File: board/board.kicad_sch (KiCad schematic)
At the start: 6 parts, among them J2 100_digital_IO, J3 SWD_6_Pol_Needle, J4 100_digital_IO

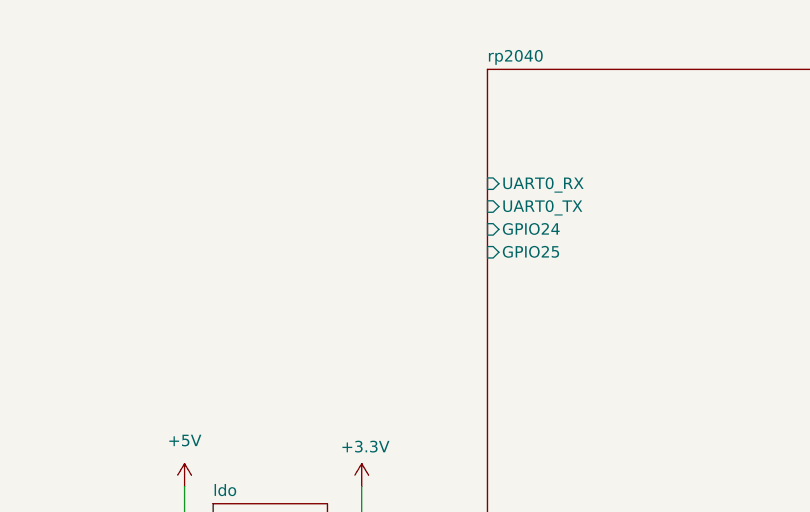
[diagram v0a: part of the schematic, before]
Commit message: added boot select button
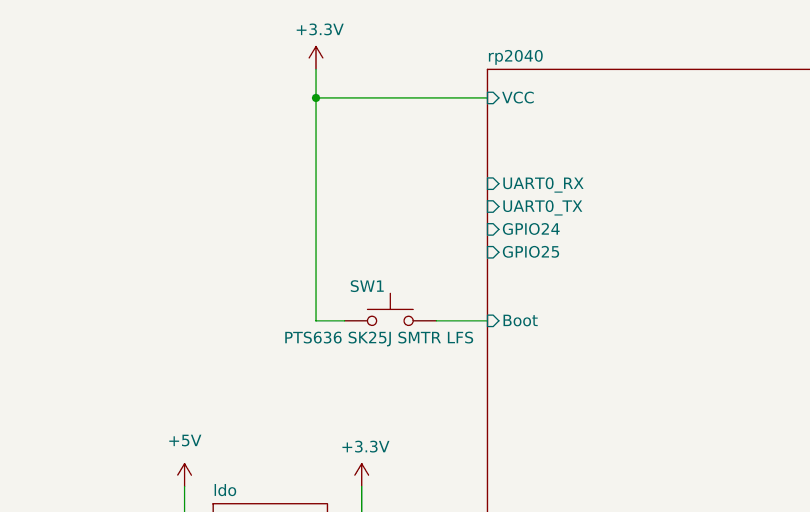
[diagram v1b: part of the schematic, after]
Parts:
- added SW1: PTS636 SK25J SMTR LFS, Resistor_SMD:R_2512_6332Metric, symbol Switch:SW_Push
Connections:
- net +3V3: now also SW1.1
- new net rp2040/Boot: SW1.2
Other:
- sheet rp2040 ports: added Boot, VCC; removed none
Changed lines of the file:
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@@
   (junction (at 74.295 100.965) (diameter 0) (color 0 0 0 0)
+  )
+  (junction (at 86.36 25.4) (diameter 0) (color 0 0 0 0)
   )
   (junction (at 71.755 73.025) (diameter 0) (color 0 0 0 0)
@@
     (stroke (width 0) (type default))
   )
+  (wire (pts (xy 86.36 22.225) (xy 86.36 25.4))
+    (stroke (width 0) (type default))
+  )
   (wire (pts (xy 167.64 43.815) (xy 227.33 43.815))
     (stroke (width 0) (type default))
@@
     (stroke (width 0) (type default))
   )
+  (wire (pts (xy 86.36 25.4) (xy 105.41 25.4))
+    (stroke (width 0) (type default))
+  )
   (wire (pts (xy 74.295 100.965) (xy 74.295 78.105))
     (stroke (width 0) (type default))
@@
     (stroke (width 0) (type default))
   )
+  (wire (pts (xy 89.535 50.165) (xy 86.36 50.165))
+    (stroke (width 0) (type default))
+  )
   (wire (pts (xy 48.895 151.765) (xy 48.895 146.685))
     (stroke (width 0) (type default))
@@
     (stroke (width 0) (type default))
   )
+  (wire (pts (xy 99.695 50.165) (xy 105.41 50.165))
+    (stroke (width 0) (type default))
+  )
   (wire (pts (xy 32.385 149.225) (xy 51.435 149.225))
     (stroke (width 0) (type default))
@@
   )
   (wire (pts (xy 189.23 46.355) (xy 225.425 46.355))
+    (stroke (width 0) (type default))
+  )
+  (wire (pts (xy 86.36 50.165) (xy 86.36 25.4))
     (stroke (width 0) (type default))
   )
@@
         (path "/57732dd3-1162-4c3f-88bd-31bf473d124d"
           (reference "J3") (unit 1)
+        )
+      )
+    )
+  )
+  (symbol (lib_id "Switch:SW_Push") (at 94.615 50.165 0) (unit 1)
+    (in_bom yes) (on_board yes) (dnp no)
+    (property "Reference" "SW1" (at 92.075 46.355 0)
+      (effects (font (size 1.27 1.27)))
+    )
+    (property "Value" "PTS636 SK25J SMTR LFS" (at 93.345 52.07 0)
+      (effects (font (size 1.27 1.27)))
+    )
+    (property "Footprint" "Resistor_SMD:R_2512_6332Metric" (at 94.615 45.085 0)
+      (effects (font (size 1.27 1.27)) hide)
+    )
+    (property "Datasheet" "~" (at 94.615 45.085 0)
+      (effects (font (size 1.27 1.27)) hide)
+    )
+    (property "MPN" "PTS636 SK25J SMTR LFS" (at 94.615 50.165 0)
+      (effects (font (size 1.27 1.27)) hide)
+    )
+    (pin "1")
+    (pin "2")
+    (instances
+      (project "board"
+        (path "/57732dd3-1162-4c3f-88bd-31bf473d124d"
+          (reference "SW1") (unit 1)
         )
       )
@@
     )
   )
+  (symbol (lib_id "power:+3.3V") (at 86.36 22.225 0) (unit 1)
+    (in_bom yes) (on_board yes) (dnp no)
+    (property "Reference" "#PWR010" (at 86.36 26.035 0)
+      (effects (font (size 1.27 1.27)) hide)
+    )
+    (property "Value" "+3.3V" (at 86.741 17.8308 0)
+      (effects (font (size 1.27 1.27)))
+    )
+    (property "Footprint" "" (at 86.36 22.225 0)
+      (effects (font (size 1.27 1.27)) hide)
+    )
+    (property "Datasheet" "" (at 86.36 22.225 0)
+      (effects (font (size 1.27 1.27)) hide)
+    )
+    (pin "1")
+    (instances
+      (project "board"
+        (path "/57732dd3-1162-4c3f-88bd-31bf473d124d/d7f4faf0-6611-4124-99f4-3c5e31784302"
+          (reference "#PWR010") (unit 1)
+        )
+        (path "/57732dd3-1162-4c3f-88bd-31bf473d124d"
+          (reference "#PWR01") (unit 1)
+        )
+      )
+    )
+  )
   (symbol (lib_id "power:GND") (at 250.825 100.33 0) (unit 1)
     (in_bom yes) (on_board yes) (dnp no)
@@
       (effects (font (size 1.27 1.27)) (justify left))
     )
+    (pin "VCC" input (at 105.41 25.4 180)
+      (effects (font (size 1.27 1.27)) (justify left))
+    )
+    (pin "Boot" input (at 105.41 50.165 180)
+      (effects (font (size 1.27 1.27)) (justify left))
+    )

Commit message: fixed boot select circuit
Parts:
- added R1: 1k, Resistor_SMD:R_0603_1608Metric, symbol Device:R_Small
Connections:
- net +3V3: no longer SW1.1
- net GND: now also SW1.1
- net rp2040/Boot: now also R1.2; no longer SW1.2
- new net: R1.1, SW1.2
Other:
- moved on the sheet: SW1
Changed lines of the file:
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@@
   (junction (at 74.295 100.965) (diameter 0) (color 0 0 0 0)
-  )
-  (junction (at 86.36 25.4) (diameter 0) (color 0 0 0 0)
   )
   (junction (at 71.755 73.025) (diameter 0) (color 0 0 0 0)
@@
     (stroke (width 0) (type default))
   )
+  (wire (pts (xy 101.6 50.165) (xy 105.41 50.165))
+    (stroke (width 0) (type default))
+  )
   (wire (pts (xy 74.295 100.965) (xy 70.485 100.965))
     (stroke (width 0) (type default))
   )
-  (wire (pts (xy 89.535 50.165) (xy 86.36 50.165))
-    (stroke (width 0) (type default))
-  )
   (wire (pts (xy 48.895 151.765) (xy 48.895 146.685))
     (stroke (width 0) (type default))
@@
     (stroke (width 0) (type default))
   )
-  (wire (pts (xy 99.695 50.165) (xy 105.41 50.165))
+  (wire (pts (xy 79.375 50.165) (xy 81.28 50.165))
     (stroke (width 0) (type default))
   )
@@
     (stroke (width 0) (type default))
   )
-  (wire (pts (xy 86.36 50.165) (xy 86.36 25.4))
-    (stroke (width 0) (type default))
-  )
   (wire (pts (xy 229.235 83.185) (xy 229.235 41.275))
     (stroke (width 0) (type default))
@@
     (stroke (width 0) (type default))
   )
+  (wire (pts (xy 79.375 54.61) (xy 79.375 50.165))
+    (stroke (width 0) (type default))
+  )
   (wire (pts (xy 250.825 55.245) (xy 250.825 58.42))
     (stroke (width 0) (type default))
@@
   )
   (wire (pts (xy 74.295 107.95) (xy 74.295 100.965))
+    (stroke (width 0) (type default))
+  )
+  (wire (pts (xy 91.44 50.165) (xy 96.52 50.165))
     (stroke (width 0) (type default))
   )
@@
     )
   )
-  (symbol (lib_id "Switch:SW_Push") (at 94.615 50.165 0) (unit 1)
+  (symbol (lib_id "Switch:SW_Push") (at 86.36 50.165 0) (unit 1)
     (in_bom yes) (on_board yes) (dnp no)
-    (property "Reference" "SW1" (at 92.075 46.355 0)
-      (effects (font (size 1.27 1.27)))
-    )
-    (property "Value" "PTS636 SK25J SMTR LFS" (at 93.345 52.07 0)
-      (effects (font (size 1.27 1.27)))
-    )
-    (property "Footprint" "Resistor_SMD:R_2512_6332Metric" (at 94.615 45.085 0)
-      (effects (font (size 1.27 1.27)) hide)
-    )
-    (property "Datasheet" "~" (at 94.615 45.085 0)
-      (effects (font (size 1.27 1.27)) hide)
-    )
-    (property "MPN" "PTS636 SK25J SMTR LFS" (at 94.615 50.165 0)
+    (property "Reference" "SW1" (at 83.82 46.355 0)
+      (effects (font (size 1.27 1.27)))
+    )
+    (property "Value" "PTS636 SK25J SMTR LFS" (at 85.09 52.07 0)
+      (effects (font (size 1.27 1.27)))
+    )
+    (property "Footprint" "Resistor_SMD:R_2512_6332Metric" (at 86.36 45.085 0)
+      (effects (font (size 1.27 1.27)) hide)
+    )
+    (property "Datasheet" "~" (at 86.36 45.085 0)
+      (effects (font (size 1.27 1.27)) hide)
+    )
+    (property "MPN" "PTS636 SK25J SMTR LFS" (at 86.36 50.165 0)
       (effects (font (size 1.27 1.27)) hide)
     )
@@
     )
   )
+  (symbol (lib_id "Device:R_Small") (at 99.06 50.165 90) (mirror x) (unit 1)
+    (in_bom yes) (on_board yes) (dnp no)
+    (property "Reference" "R1" (at 99.695 48.26 90)
+      (effects (font (size 1.27 1.27)))
+    )
+    (property "Value" "1k" (at 99.06 53.975 90)
+      (effects (font (size 1.27 1.27)))
+    )
+    (property "Footprint" "Resistor_SMD:R_0603_1608Metric" (at 99.06 50.165 0)
+      (effects (font (size 1.27 1.27)) hide)
+    )
+    (property "Datasheet" "~" (at 99.06 50.165 0)
+      (effects (font (size 1.27 1.27)) hide)
+    )
+    (pin "1")
+    (pin "2")
+    (instances
+      (project "board"
+        (path "/57732dd3-1162-4c3f-88bd-31bf473d124d"
+          (reference "R1") (unit 1)
+        )
+      )
+    )
+  )
   (symbol (lib_id "power:+3.3V") (at 32.385 146.685 0) (unit 1)
     (in_bom yes) (on_board yes) (dnp no)
@@
         )
       )
+    )
+  )
+  (symbol (lib_id "power:GND") (at 79.375 54.61 0) (unit 1)
+    (in_bom yes) (on_board yes) (dnp no) (fields_autoplaced)
+    (property "Reference" "#PWR02" (at 79.375 60.96 0)
+      (effects (font (size 1.27 1.27)) hide)
+    )
+    (property "Value" "GND" (at 79.375 59.69 0)
+      (effects (font (size 1.27 1.27)))
+    )
+    (property "Footprint" "" (at 79.375 54.61 0)
+      (effects (font (size 1.27 1.27)) hide)
+    )
+    (property "Datasheet" "" (at 79.375 54.61 0)
+      (effects (font (size 1.27 1.27)) hide)
+    )
+    (pin "1")
+    (instances
+      (project "board"
+        (path "/57732dd3-1162-4c3f-88bd-31bf473d124d"
+          (reference "#PWR02") (unit 1)
+        )
+      )

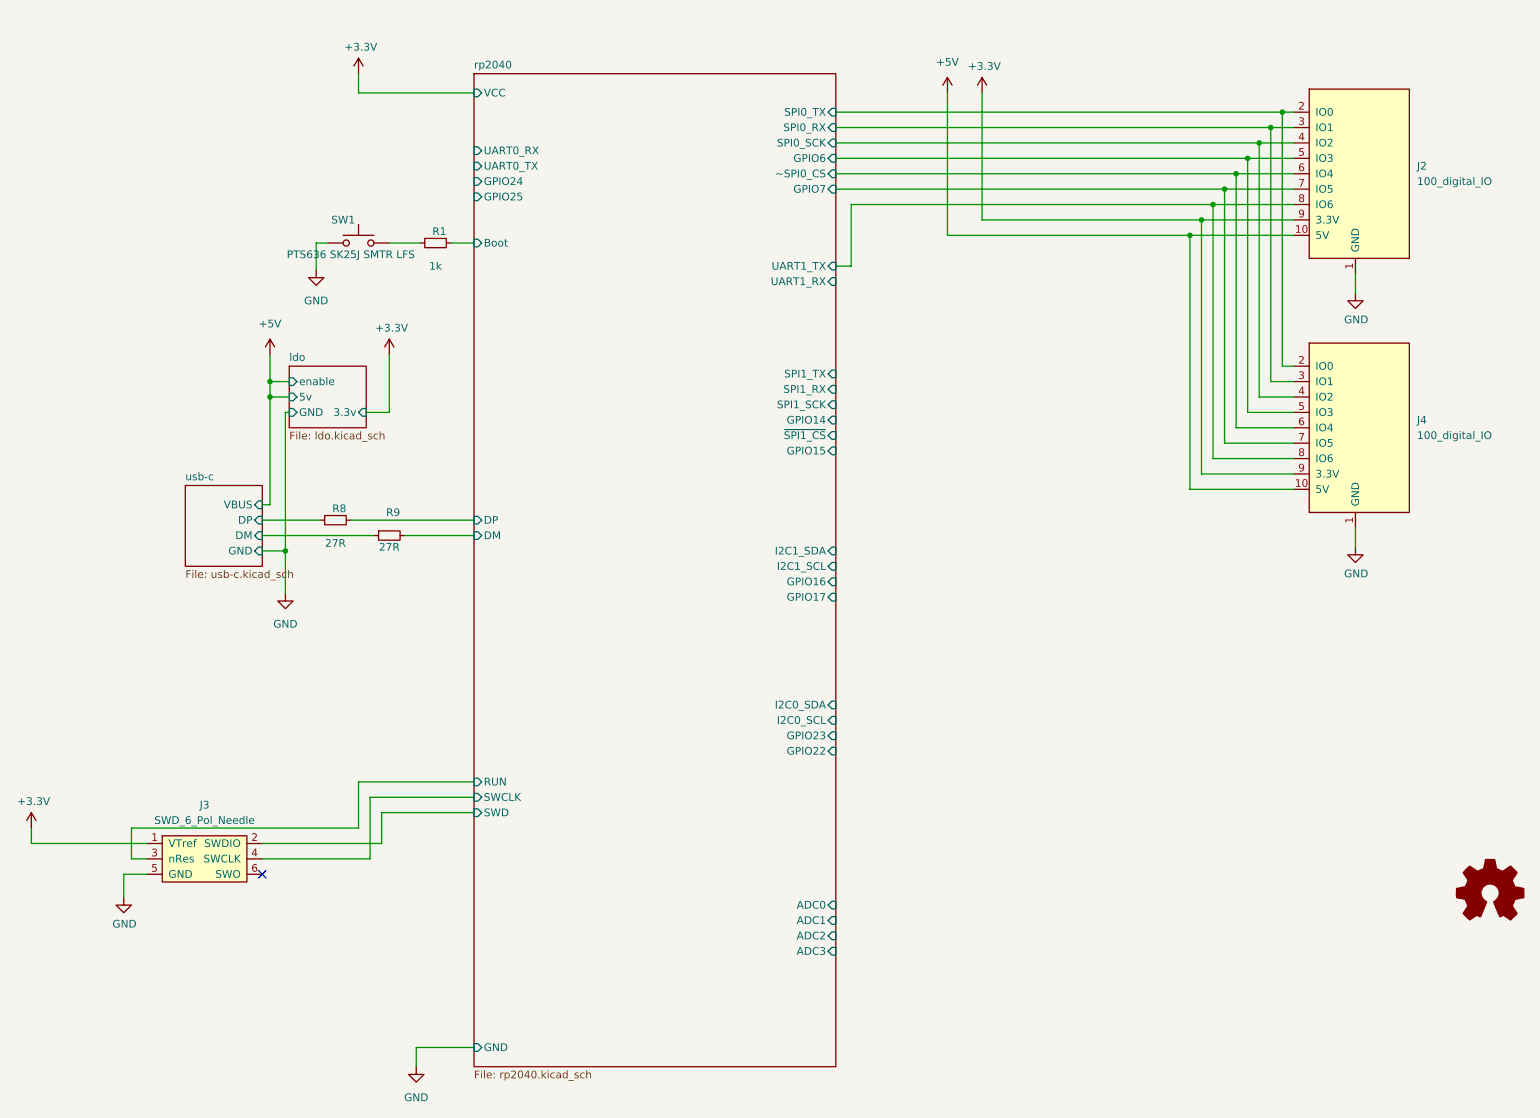
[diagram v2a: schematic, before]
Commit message: added straping support for different interfaces
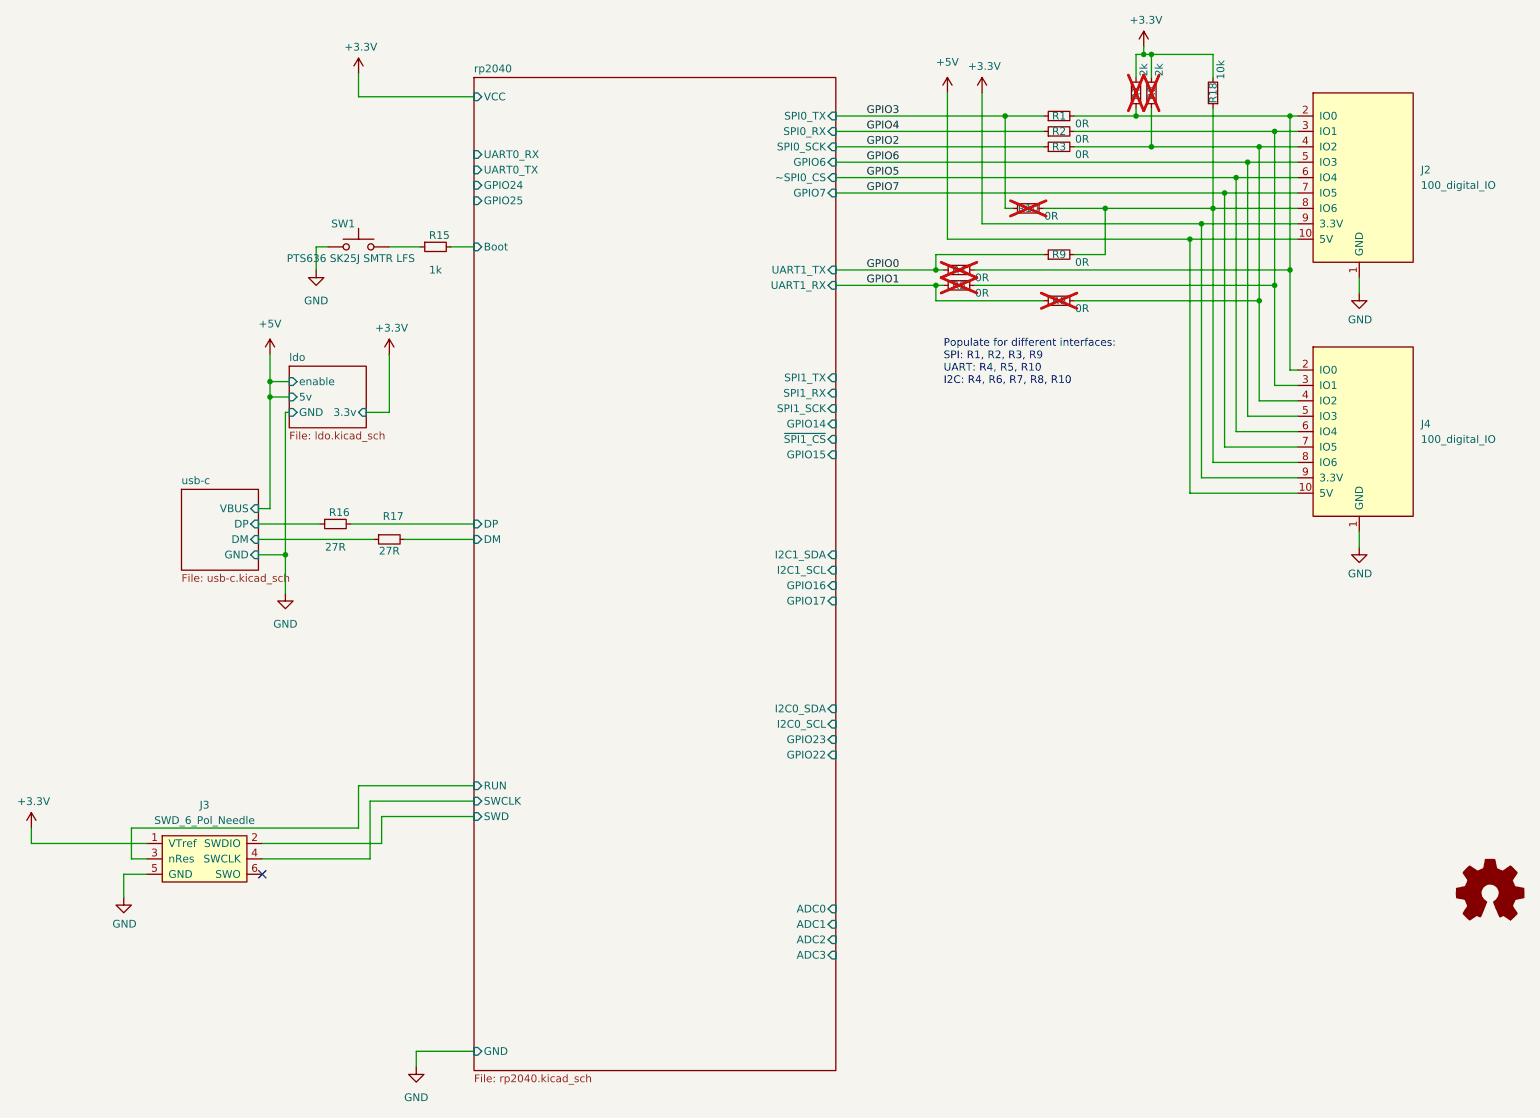
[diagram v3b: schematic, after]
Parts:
- added R1, R10, R2, R3, R4, R5, R6, R9: 0R, Resistor_SMD:R_0603_1608Metric, symbol Device:R_Small
- added R18: 10k, Resistor_SMD:R_0603_1608Metric, symbol Device:R_Small
- added R7, R8: 2k, Resistor_SMD:R_0603_1608Metric, symbol Device:R_Small
- renumbered R1 to R15, R8 to R16, R9 to R17
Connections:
- net +3V3: now also R18.2, R7.2, R8.2
- net rp2040/GPIO6 renamed GPIO6
- net rp2040/GPIO7 renamed GPIO7
- net rp2040/SPI0_RX: no longer names the net of J2.3 (IO1), J4.3 (IO1)
- net rp2040/SPI0_RX: now also R2.2, R5.2
- net rp2040/SPI0_SCK: no longer names the net of J2.4 (IO2), J4.4 (IO2)
- net rp2040/SPI0_SCK: now also R3.2, R6.2, R8.1
- net rp2040/SPI0_TX: no longer names the net of J2.2 (IO0), J4.2 (IO0)
- net rp2040/SPI0_TX: now also R1.2, R4.2, R7.1
- net rp2040/UART1_TX: no longer names the net of J2.8 (IO6), J4.8 (IO6)
- net rp2040/UART1_TX: now also R10.2, R18.1, R9.2
- net rp2040/~SPI0_CS renamed GPIO5
- new net GPIO0: R4.1, R9.1
- new net GPIO1: R5.1, R6.1
- new net GPIO2: R3.1
- new net GPIO3: R1.1, R10.1
- new net GPIO4: R2.1
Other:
- note added: "Populate for different interfaces: SPI: R1, R2, R3, R9 UART: R4, R5, R10 I2C: R4, R6, R7, R8, R10"
- moved on the sheet: J2, J4, R15, R16, R17, SW1
